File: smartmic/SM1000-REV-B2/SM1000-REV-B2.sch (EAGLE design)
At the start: 174 parts, among them CN1 HDR100-3, CN10 MJ-3523-SMT, CN11 HDR100-3, CN12 DF11-16DS, CN2 MOLEX-MINI-B-SMT, CN3 RASM712PX, CN4 RJ-45, CN5 MJ-3523-SMT, CN6 MJ-3523-SMT, CN7 MJ-3523-SMT, CN8 MJ-3523-SMT, CN9 MJ-3523-SMT, J1 JMP-2PIN, J3 JMP-2PIN, J4 JMP-2PIN, J5 JMP-2PIN, P1 TPAD50, P10 TPAD50, P11 TPAD50, P12 TPAD50, P13 TPAD50, P14 TPAD50, P15 TPAD50, P16 TPAD50, P17 TPAD50, P18 TPAD50, P19 TPAD50, P2 TPAD50, P20 TPAD50, P3 TPAD50, P4 TPAD50, P5 TPAD50, P6 TPAD50, P7 TPAD50, P8 TPAD50, P9 TPAD50, SW1 SW-BOURNS-7914S, SW2 SW-BOURNS-7914S, SW3 DPDT, SW4 SW-BOURNS-7914S, T1 SM-LP-5001, T2 SM-LP-5001, U1 STM32F405, U2 LD3985M33R, U3 STMPS2141, U4 EMIF02-USB03F2, U5 TPS54329E, U6 LMV341, U7 LMV341, U8 LM386M-1, U9 LMV341

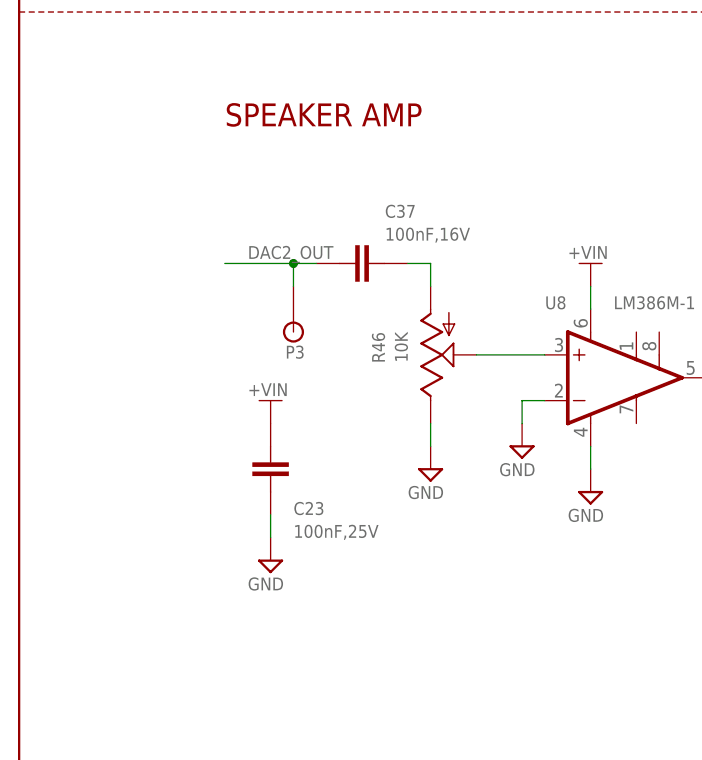
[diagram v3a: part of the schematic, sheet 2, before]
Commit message: Implemented Davids changes(21, 22 & 23) to schematic. Parts are in PCB, but not placed. RGB Updated Change Log RGB
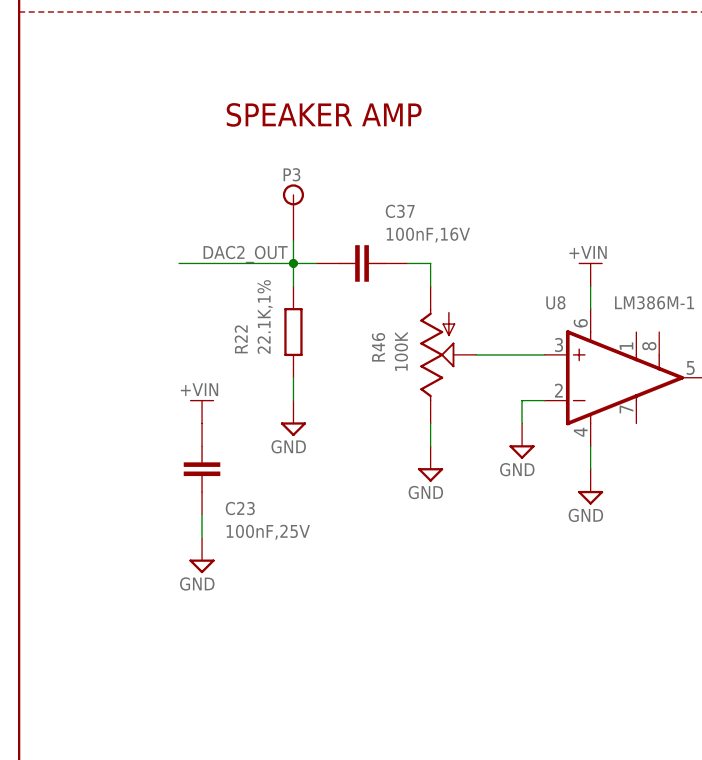
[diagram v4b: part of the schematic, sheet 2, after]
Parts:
- added R22: 22.1K,1%, AA-ipc-7351-resistor:RESISTOR_0603
- R46: value 10K -> 100K
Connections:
- net DAC2_OUT: now also R22.2
- net GND: now also R22.1
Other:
- moved on the sheet: C23, P3
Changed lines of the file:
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@@
 <part name="R24" library="AA-ipc-7351-resistor" deviceset="RESISTOR_" device="0603" value="47K,1%"/>
 <part name="V40" library="A-SUPPLY2" deviceset="GND" device=""/>
-<part name="R46" library="_RoweTel" deviceset="POT-3310C" device="" value="10K"/>
+<part name="R46" library="_RoweTel" deviceset="POT-3310C" device="" value="100K"/>
 <part name="SW3" library="_RoweTel" deviceset="SW-PWR-E-SWITCH" device="" value="DPDT"/>
 <part name="C26" library="ipc-7351-capacitor" deviceset="CAPACITOR_" device="0603" value="100nF,25V"/>
@@
 <part name="C49" library="AA-ipc-7351-capacitor" deviceset="CAPACITOR_" device="0603" value="100nF,16V"/>
 <part name="V124" library="A-SUPPLY2" deviceset="GND" device=""/>
+<part name="R22" library="AA-ipc-7351-resistor" deviceset="RESISTOR_" device="0603" value="22.1K,1%"/>
+<part name="V125" library="A-SUPPLY2" deviceset="GND" device=""/>
 </parts>
 <sheets>
@@
 <attribute name="VALUE" x="109.22" y="167.64" size="1.4224" layer="96"/>
 </instance>
-<instance part="C23" gate="G$1" x="25.4" y="45.72" smashed="yes" rot="R270">
-<attribute name="NAME" x="27.94" y="40.64" size="1.4224" layer="95" ratio="9"/>
-<attribute name="VALUE" x="27.94" y="38.1" size="1.4224" layer="96" ratio="9"/>
+<instance part="C23" gate="G$1" x="17.78" y="45.72" smashed="yes" rot="R270">
+<attribute name="NAME" x="20.32" y="40.64" size="1.4224" layer="95" ratio="9"/>
+<attribute name="VALUE" x="20.32" y="38.1" size="1.4224" layer="96" ratio="9"/>
 </instance>
 <instance part="C41" gate="G$1" x="162.56" y="162.56" smashed="yes" rot="R270">
@@
 <attribute name="VALUE" x="121.92" y="161.798" size="1.4224" layer="96" ratio="9"/>
 </instance>
-<instance part="U$12" gate="G$1" x="25.4" y="53.34" smashed="yes">
-<attribute name="VALUE" x="22.86" y="53.848" size="1.4224" layer="95" ratio="9"/>
-</instance>
-<instance part="V6" gate="GND" x="25.4" y="35.56" smashed="yes">
-<attribute name="VALUE" x="22.86" y="32.258" size="1.4224" layer="96" ratio="9"/>
+<instance part="U$12" gate="G$1" x="17.78" y="53.34" smashed="yes">
+<attribute name="VALUE" x="15.24" y="53.848" size="1.4224" layer="95" ratio="9"/>
+</instance>
+<instance part="V6" gate="GND" x="17.78" y="35.56" smashed="yes">
+<attribute name="VALUE" x="15.24" y="32.258" size="1.4224" layer="96" ratio="9"/>
 </instance>
 <instance part="V90" gate="GND" x="162.56" y="58.42" smashed="yes">
@@
 <instance part="P1" gate="G$1" x="170.18" y="127" rot="R180"/>
 <instance part="P2" gate="G$1" x="170.18" y="83.82" rot="R180"/>
-<instance part="P3" gate="G$1" x="27.94" y="66.04" rot="R180"/>
+<instance part="P3" gate="G$1" x="27.94" y="71.12"/>
 <instance part="P4" gate="G$1" x="129.54" y="127" rot="R180"/>
 <instance part="C1" gate="G$1" x="101.6" y="251.46" smashed="yes" rot="R90">
@@
 </instance>
 <instance part="R21" gate="G$1" x="91.44" y="259.08"/>
+<instance part="R22" gate="G$1" x="27.94" y="60.96" smashed="yes" rot="R90">
+<attribute name="NAME" x="22.86" y="58.42" size="1.4224" layer="95" ratio="9" rot="R90"/>
+<attribute name="VALUE" x="25.4" y="58.42" size="1.4224" layer="96" ratio="9" rot="R90"/>
+</instance>
+<instance part="V125" gate="GND" x="27.94" y="50.8" smashed="yes">
+<attribute name="VALUE" x="25.4" y="47.498" size="1.4224" layer="96" ratio="9"/>
+</instance>
 </instances>
 <busses>
@@
 <segment>
 <pinref part="C23" gate="G$1" pin="2"/>
-<wire x1="25.4" y1="40.64" x2="25.4" y2="38.1" width="0.1524" layer="91"/>
+<wire x1="17.78" y1="40.64" x2="17.78" y2="38.1" width="0.1524" layer="91"/>
 <pinref part="V6" gate="GND" pin="GND"/>
 </segment>
@@
 <wire x1="35.56" y1="246.38" x2="35.56" y2="243.84" width="0.1524" layer="91"/>
 <pinref part="V122" gate="GND" pin="GND"/>
+</segment>
+<segment>
+<pinref part="R22" gate="G$1" pin="1"/>
+<wire x1="27.94" y1="55.88" x2="27.94" y2="53.34" width="0.1524" layer="91"/>
+<pinref part="V125" gate="GND" pin="GND"/>
 </segment>
 </net>
@@
 <pinref part="C37" gate="G$1" pin="1"/>
 <wire x1="30.48" y1="68.58" x2="27.94" y2="68.58" width="0.1524" layer="91"/>
-<wire x1="27.94" y1="68.58" x2="27.94" y2="66.04" width="0.1524" layer="91"/>
-<label x="22.86" y="69.088" size="1.4224" layer="95" ratio="10"/>
+<wire x1="27.94" y1="68.58" x2="27.94" y2="71.12" width="0.1524" layer="91"/>
+<label x="17.78" y="69.088" size="1.4224" layer="95" ratio="10"/>
 <pinref part="P3" gate="G$1" pin="1"/>
-<wire x1="27.94" y1="68.58" x2="20.32" y2="68.58" width="0.1524" layer="91"/>
+<wire x1="27.94" y1="68.58" x2="15.24" y2="68.58" width="0.1524" layer="91"/>
 <junction x="27.94" y="68.58"/>
-</segment>
-</net>
+<pinref part="R22" gate="G$1" pin="2"/>
+<wire x1="27.94" y1="66.04" x2="27.94" y2="68.58" width="0.1524" layer="91"/>
+</segment>
+</net>
